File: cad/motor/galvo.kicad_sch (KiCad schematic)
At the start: 23 parts, among them Q1 NPN, Q10 NMOS, Q2 PMOS, Q3 NMOS, Q4 NMOS, Q5 NMOS, Q6 NPN, Q7 NMOS, Q8 NMOS, Q9 PMOS

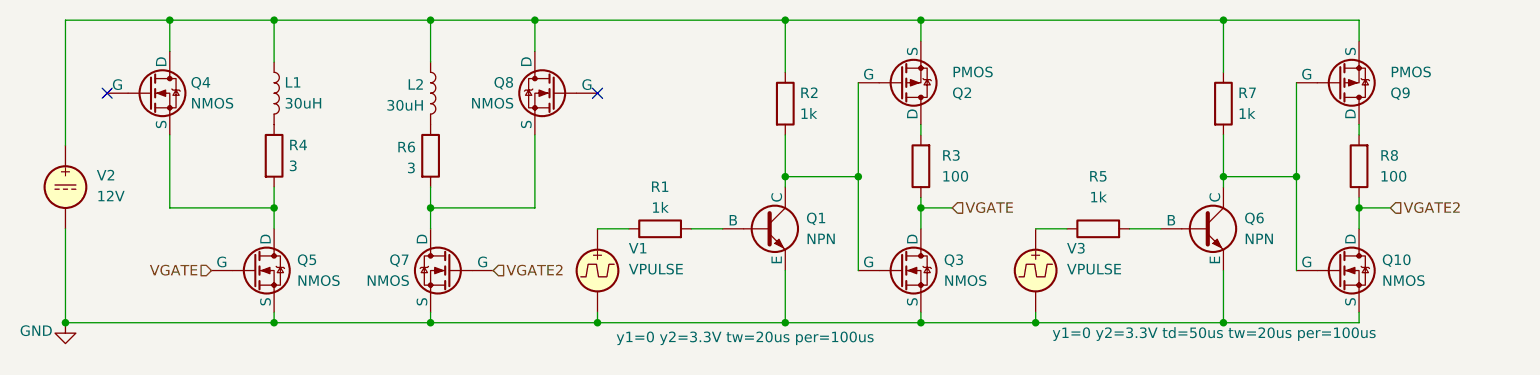
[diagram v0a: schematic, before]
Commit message: update galvo + laser driver
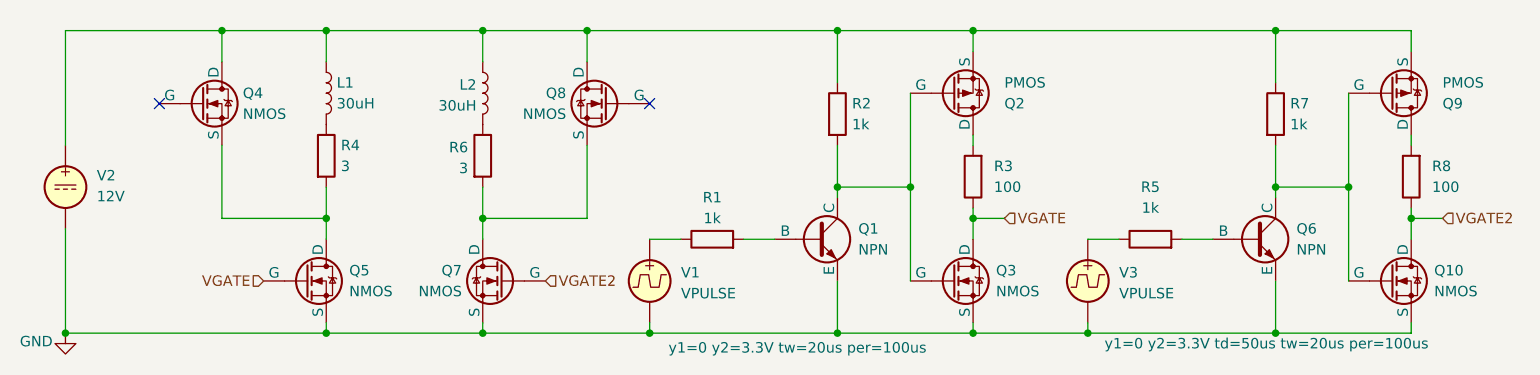
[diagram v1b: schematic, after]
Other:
- moved on the sheet: L1, L2, Q1, Q10, Q2, Q3, Q4, Q5, Q6, Q7, Q8, Q9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
